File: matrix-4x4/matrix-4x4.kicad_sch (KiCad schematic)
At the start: 39 parts

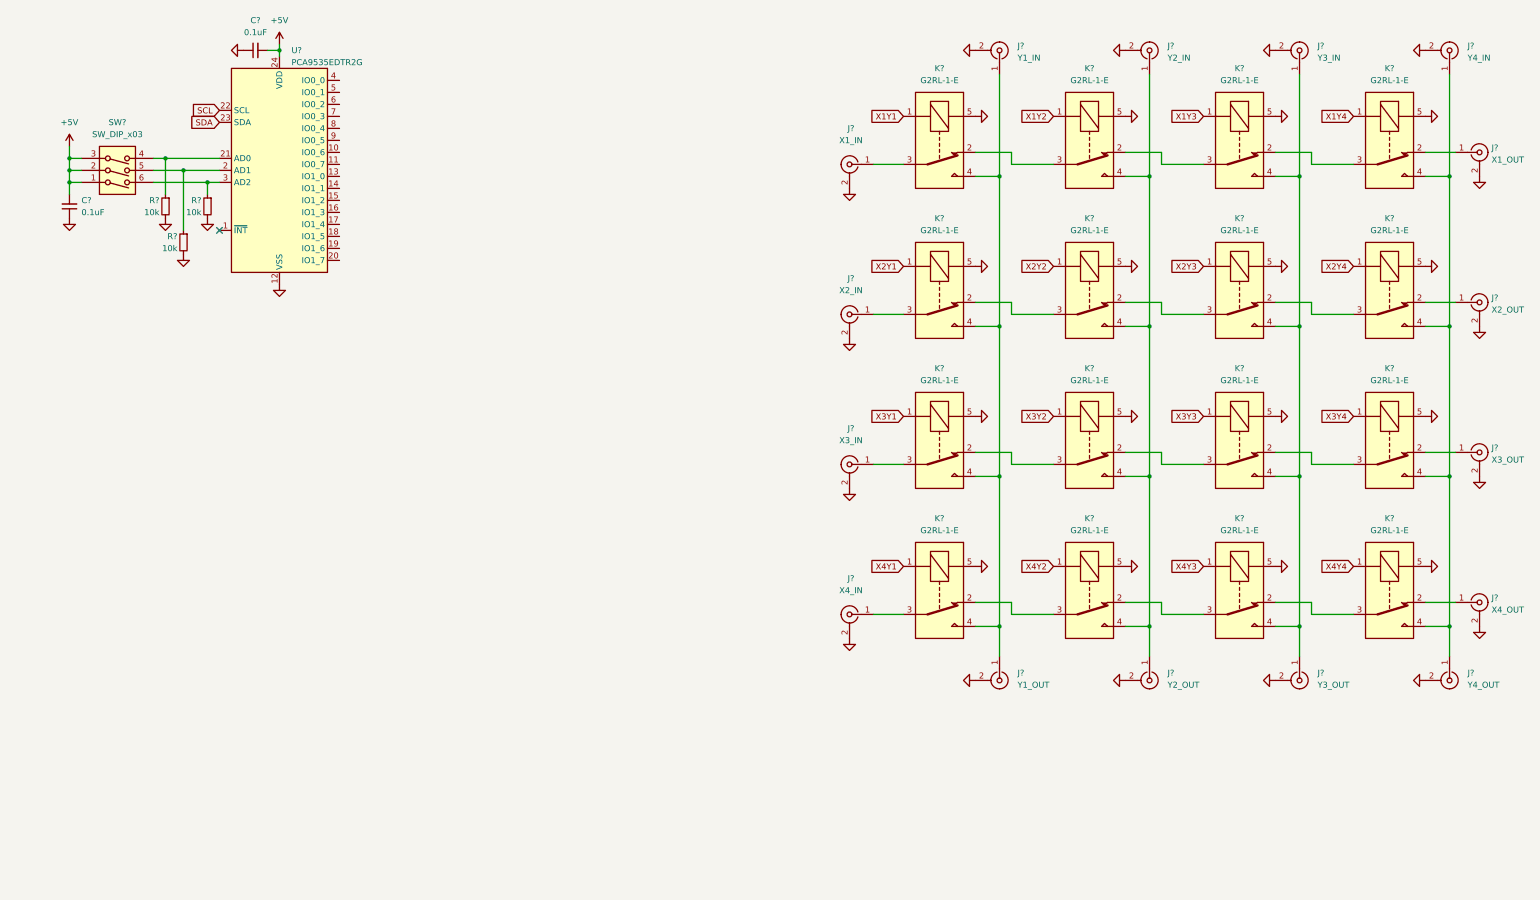
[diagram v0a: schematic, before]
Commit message: finalized single-point switch design, more work on 4x4 matrix
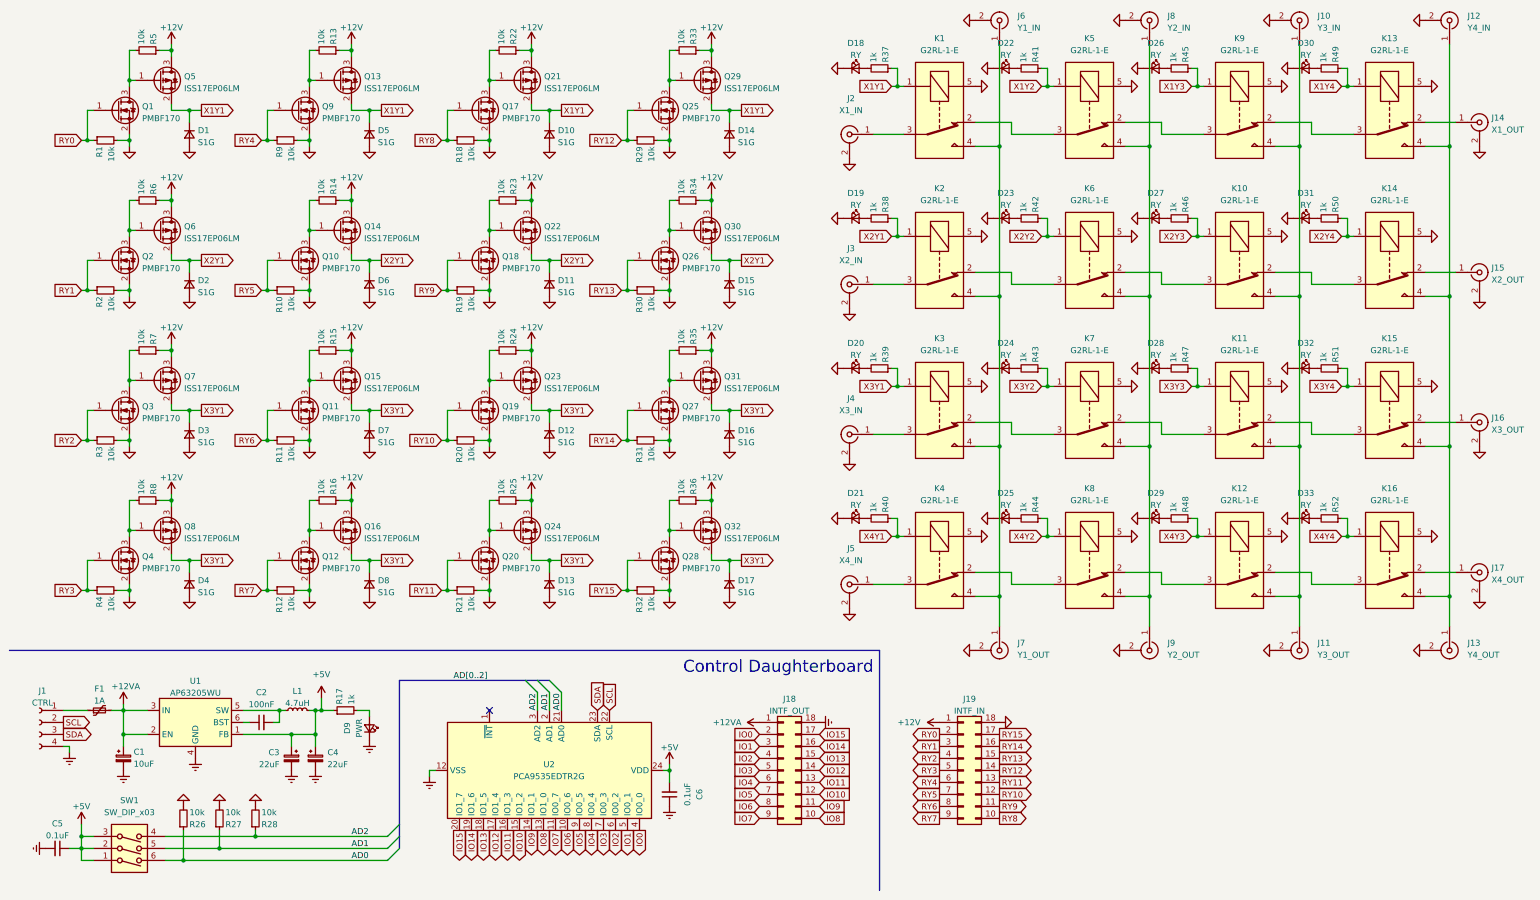
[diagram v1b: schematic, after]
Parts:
- added C1: 10uF, Capacitor_Tantalum_SMD:CP_EIA-3528-15_AVX-H_Pad1.50x2.35mm_HandSolder, symbol Device:C_Polarized_Small
- added C2: 100nF, Capacitor_SMD:C_0805_2012Metric_Pad1.18x1.45mm_HandSolder, symbol Device:C_Small
- added C3, C4: 22uF, Capacitor_Tantalum_SMD:CP_EIA-3528-15_AVX-H_Pad1.50x2.35mm_HandSolder, symbol Device:C_Polarized_Small
- added D1, D10, D11, D12, D13, D14, D15, D16, D17, D2, D3, D4, D5, D6, D7, D8: S1G, Diode_SMD:D_SMA, symbol Device:D_Small
- added D18, D19, D20, D21, D22, D23, D24, D25, D26, D27, D28, D29, D30, D31, D32, D33: RY, LED_SMD:LED_0805_2012Metric_Pad1.15x1.40mm_HandSolder, symbol Device:LED_Small
- added D9: PWR, LED_SMD:LED_0805_2012Metric_Pad1.15x1.40mm_HandSolder, symbol Device:LED_Small
- added F1: 1A, Fuse:Fuse_1206_3216Metric_Pad1.42x1.75mm_HandSolder, symbol Device:Polyfuse_Small
- added J1: CTRL, Connector_PinHeader_2.54mm:PinHeader_1x04_P2.54mm_Vertical, symbol Connector:Conn_01x04_Female
- added J18: INTF_OUT, Connector_PinHeader_2.00mm:PinHeader_2x09_P2.00mm_Vertical, symbol Connector_Generic:Conn_02x09_Counter_Clockwise
- added J19: INTF_IN, Connector_PinSocket_2.00mm:PinSocket_2x09_P2.00mm_Vertical, symbol Connector_Generic:Conn_02x09_Counter_Clockwise
- added L1: 4.7uH, Inductor_SMD:L_Taiyo-Yuden_NR-30xx_HandSoldering, symbol Device:L_Small
- added Q1, Q10, Q11, Q12, Q17, Q18, Q19, Q2, Q20, Q25, Q26, Q27, Q28, Q3, Q4, Q9: PMBF170, Package_TO_SOT_SMD:SOT-23_Handsoldering, symbol Transistor_FET:BS170F
- added Q13, Q14, Q15, Q16, Q21, Q22, Q23, Q24, Q29, Q30, Q31, Q32, Q5, Q6, Q7, Q8: ISS17EP06LM, Package_TO_SOT_SMD:SOT-23_Handsoldering, symbol Device:Q_PMOS_GSD
- added R1, R10, R11, R12, R13, R14, R15, R16, R18, R19, R2, R20, R21, R22, R23, R24, R25, R29, R3, R30, R31, R32, R33, R34, R35, R36, R4, R5, R6, R7, R8, R9: 10k, Resistor_SMD:R_0805_2012Metric_Pad1.20x1.40mm_HandSolder, symbol Device:R_Small
- added R17, R37, R38, R39, R40, R41, R42, R43, R44, R45, R46, R47, R48, R49, R50, R51, R52: 1k, Resistor_SMD:R_0805_2012Metric_Pad1.20x1.40mm_HandSolder, symbol Device:R_Small
- added U1: AP63205WU, Package_TO_SOT_SMD:TSOT-23-6, symbol Regulator_Switching:AP63205WU
- C5, C6: renamed from C?; footprint (none) -> Capacitor_SMD:C_0805_2012Metric_Pad1.18x1.45mm_HandSolder
- J10, J11, J12, J13, J14, J15, J16, J17, J2, J3, J4, J5, J6, J7, J8, J9: renamed from J?; footprint (none) -> conn:Coax_Edge_2.54_1.27
- R26, R27, R28: renamed from R?; footprint (none) -> Resistor_SMD:R_0805_2012Metric_Pad1.20x1.40mm_HandSolder
- SW1: renamed from SW?; footprint (none) -> Button_Switch_THT:SW_DIP_SPSTx03_Slide_6.7x9.18mm_W7.62mm_P2.54mm_LowProfile
- U2: renamed from U?; footprint (none) -> Package_SO:SOIC-24W_7.5x15.4mm_P1.27mm
- gave numbers to parts that had none: 16
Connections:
- net +5V: now also C5.1, C3.1, C4.1, L1.2, R17.1, U1.1 (FB); no longer C5.2
- net GND: now also D1.2 (A), D10.2 (A), D11.2 (A), D12.2 (A), D13.2 (A), D14.2 (A), D15.2 (A), D16.2 (A), D17.2 (A), D18.1 (K), D19.1 (K), D2.2 (A), D20.1 (K), D21.1 (K), D22.1 (K), D23.1 (K), D24.1 (K), D25.1 (K), D26.1 (K), D27.1 (K), D28.1 (K), D29.1 (K), D3.2 (A), D30.1 (K), D31.1 (K), D32.1 (K), D33.1 (K), D4.2 (A), D5.2 (A), D6.2 (A), D7.2 (A), D8.2 (A), J19.18 (Pin_18), Q1.2 (S), Q10.2 (S), Q11.2 (S), Q12.2 (S), Q17.2 (S), Q18.2 (S), Q19.2 (S), Q2.2 (S), Q20.2 (S), Q25.2 (S), Q26.2 (S), Q27.2 (S), Q28.2 (S), Q3.2 (S), Q4.2 (S), Q9.2 (S), R1.2, R10.2, R11.2, R12.2, R18.2, R19.2, R2.2, R20.2, R21.2, R29.2, R3.2, R30.2, R31.2, R32.2, R4.2, R9.2; no longer C5.1, C6.1, U2.12 (VSS)
- net SCL: now also J1.2 (Pin_2)
- net SDA: now also J1.3 (Pin_3)
- net X1Y1: now also D1.1 (K), D10.1 (K), D14.1 (K), D5.1 (K), Q13.2 (S), Q21.2 (S), Q29.2 (S), Q5.2 (S), R37.1
- net X1Y2: now also R41.1
- net X1Y3: now also R45.1
- net X1Y4: now also R49.1
- net X2Y1: now also D11.1 (K), D15.1 (K), D2.1 (K), D6.1 (K), Q14.2 (S), Q22.2 (S), Q30.2 (S), Q6.2 (S), R38.1
- net X2Y2: now also R42.1
- net X2Y3: now also R46.1
- net X2Y4: now also R50.1
- net X3Y1: now also D12.1 (K), D13.1 (K), D16.1 (K), D17.1 (K), D3.1 (K), D4.1 (K), D7.1 (K), D8.1 (K), Q15.2 (S), Q16.2 (S), Q23.2 (S), Q24.2 (S), Q31.2 (S), Q32.2 (S), Q7.2 (S), Q8.2 (S), R39.1
- net X3Y2: now also R43.1
- net X3Y3: now also R47.1
- net X3Y4: now also R51.1
- net X4Y1: now also R40.1
- net X4Y2: now also R44.1
- net X4Y3: now also R48.1
- net X4Y4: now also R52.1
- net AD1: now reaches R27.1, SW1.5, U2.2 (AD1)
- net IO6: now reaches U2.10 (IO0_6)
- net IO6: now also J18.8 (Pin_8)
- net IO7: now reaches U2.11 (IO0_7)
- net IO7: now also J18.9 (Pin_9)
- net IO8: now reaches U2.13 (IO1_0)
- net IO8: now also J18.10 (Pin_10)
- net IO9: now reaches U2.14 (IO1_1)
- net IO9: now also J18.11 (Pin_11)
- net IO10: now reaches U2.15 (IO1_2)
- net IO10: now also J18.12 (Pin_12)
- net IO11: now reaches U2.16 (IO1_3)
- net IO11: now also J18.13 (Pin_13)
- net IO12: now reaches U2.17 (IO1_4)
- net IO12: now also J18.14 (Pin_14)
- net IO13: now reaches U2.18 (IO1_5)
- net IO13: now also J18.15 (Pin_15)
- net IO14: now reaches U2.19 (IO1_6)
- net IO14: now also J18.16 (Pin_16)
- net IO15: now reaches U2.20 (IO1_7)
- net IO15: now also J18.17 (Pin_17)
- net AD0: now reaches R26.1, U2.21 (AD0)
- net AD0: now also SW1.6; no longer SW1.4
- net AD2: now reaches R28.1, U2.3 (AD2)
- net AD2: now also SW1.4; no longer SW1.6
- net IO0: now reaches U2.4 (IO0_0)
- net IO0: now also J18.2 (Pin_2)
- net IO1: now reaches U2.5 (IO0_1)
- net IO1: now also J18.3 (Pin_3)
- net IO2: now reaches U2.6 (IO0_2)
- net IO2: now also J18.4 (Pin_4)
- net IO3: now reaches U2.7 (IO0_3)
- net IO3: now also J18.5 (Pin_5)
- net IO4: now reaches U2.8 (IO0_4)
- net IO4: now also J18.6 (Pin_6)
- net IO5: now reaches U2.9 (IO0_5)
- net IO5: now also J18.7 (Pin_7)
- new net: Q12.3 (D), Q16.1 (G), R16.2
- new net: D9.2 (A), R17.2
- new net: Q27.3 (D), Q31.1 (G), R35.2
- new net: C2.2, L1.1, U1.5 (SW)
- new net: D25.2 (A), R44.2
- new net: Q18.3 (D), Q22.1 (G), R23.2
- new net: Q10.3 (D), Q14.1 (G), R14.2
- new net: C2.1, U1.6 (BST)
- new net: D19.2 (A), R38.2
- new net: D33.2 (A), R52.2
- new net: Q3.3 (D), Q7.1 (G), R7.2
- new net: Q13.1 (G), Q9.3 (D), R13.2
- new net: D30.2 (A), R49.2
- new net: Q1.3 (D), Q5.1 (G), R5.2
- new net: Q28.3 (D), Q32.1 (G), R36.2
- new net: F1.1, J1.1 (Pin_1)
- new net: D24.2 (A), R43.2
- new net: D21.2 (A), R40.2
- new net: D29.2 (A), R48.2
- new net: D28.2 (A), R47.2
- new net: Q20.3 (D), Q24.1 (G), R25.2
- new net: D20.2 (A), R39.2
- new net: Q26.3 (D), Q30.1 (G), R34.2
- new net: Q4.3 (D), Q8.1 (G), R8.2
- new net: Q25.3 (D), Q29.1 (G), R33.2
- new net: Q17.3 (D), Q21.1 (G), R22.2
- new net: D22.2 (A), R41.2
- new net: Q19.3 (D), Q23.1 (G), R24.2
- new net: Q11.3 (D), Q15.1 (G), R15.2
- new net: D18.2 (A), R37.2
- new net: D32.2 (A), R51.2
- new net: D26.2 (A), R45.2
- new net: Q2.3 (D), Q6.1 (G), R6.2
- new net: D23.2 (A), R42.2
- new net: D27.2 (A), R46.2
- new net: D31.2 (A), R50.2
- new net +12V: J19.1 (Pin_1), Q13.3 (D), Q14.3 (D), Q15.3 (D), Q16.3 (D), Q21.3 (D), Q22.3 (D), Q23.3 (D), Q24.3 (D), Q29.3 (D), Q30.3 (D), Q31.3 (D), Q32.3 (D), Q5.3 (D), Q6.3 (D), Q7.3 (D), Q8.3 (D), R13.1, R14.1, R15.1, R16.1, R22.1, R23.1, R24.1, R25.1, R33.1, R34.1, R35.1, R36.1, R5.1, R6.1, R7.1, R8.1
- new net +12VA: C1.1, F1.2, J18.1 (Pin_1), U1.2 (EN), U1.3 (IN)
- new net GNDREF: C1.2, C3.2, C4.2, C5.2, C6.1, D9.1 (K), J1.4 (Pin_4), J18.18 (Pin_18), U1.4 (GND), U2.12 (VSS)
- new net RY0: J19.2 (Pin_2), Q1.1 (G), R1.1
- new net RY1: J19.3 (Pin_3), Q2.1 (G), R2.1
- new net RY10: J19.12 (Pin_12), Q19.1 (G), R20.1
- new net RY11: J19.13 (Pin_13), Q20.1 (G), R21.1
- new net RY12: J19.14 (Pin_14), Q25.1 (G), R29.1
- new net RY13: J19.15 (Pin_15), Q26.1 (G), R30.1
- new net RY14: J19.16 (Pin_16), Q27.1 (G), R31.1
- new net RY15: J19.17 (Pin_17), Q28.1 (G), R32.1
- new net RY2: J19.4 (Pin_4), Q3.1 (G), R3.1
- new net RY3: J19.5 (Pin_5), Q4.1 (G), R4.1
- new net RY4: J19.6 (Pin_6), Q9.1 (G), R9.1
- new net RY5: J19.7 (Pin_7), Q10.1 (G), R10.1
- new net RY6: J19.8 (Pin_8), Q11.1 (G), R11.1
- new net RY7: J19.9 (Pin_9), Q12.1 (G), R12.1
- new net RY8: J19.10 (Pin_10), Q17.1 (G), R18.1
- new net RY9: J19.11 (Pin_11), Q18.1 (G), R19.1
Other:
- note added: "Control Daughterboard"
- moved on the sheet: C5, C6, J10, J11, J12, J13, J14, J15, J16, J17, J2, J3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
